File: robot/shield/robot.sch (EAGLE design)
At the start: 18 parts, among them IC1 LM386N-1, M2 ARDUINO_R3_ICSP, X1 22-23-2021, X2 22-23-2021, X3 22-23-2031, X4 22-23-2031, X5 22-23-2051

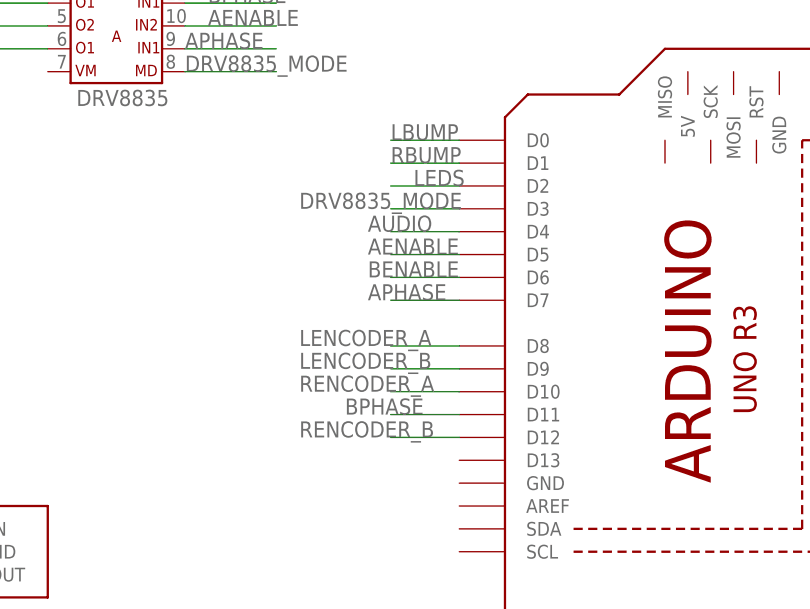
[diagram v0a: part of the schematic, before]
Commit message: Update pin assignments; layout
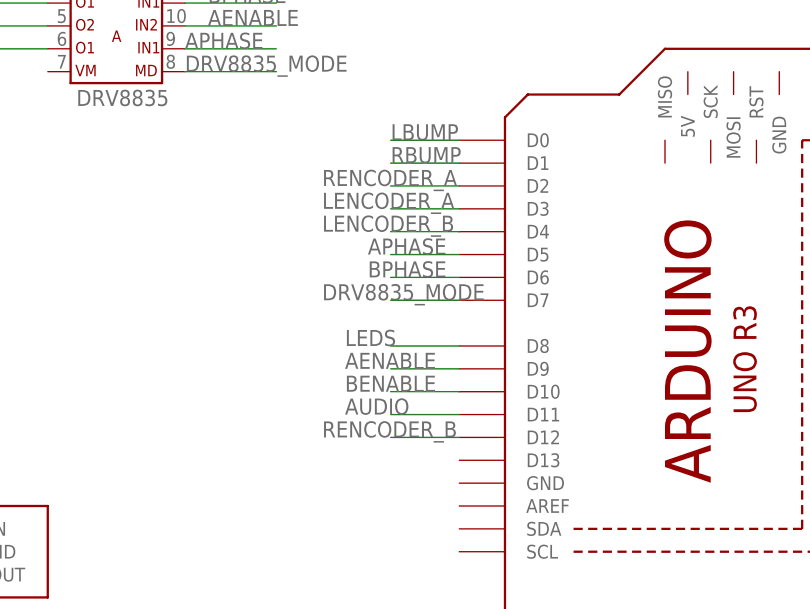
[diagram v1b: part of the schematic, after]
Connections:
- net AENABLE: now also M2.D9; no longer M2.D5
- net APHASE: now also M2.D5; no longer M2.D7
- net AUDIO: now also M2.D11; no longer M2.D4
- net BENABLE: now also M2.D10; no longer M2.D6
- net BPHASE: now also M2.D6; no longer M2.D11
- net DRV8835_MODE: now also M2.D7; no longer M2.D3
- net LEDS: now also M2.D8; no longer M2.D2
- net LENCODER_A: now also M2.D3; no longer M2.D8
- net LENCODER_B: now also M2.D4; no longer M2.D9
- net RENCODER_A: now also M2.D2; no longer M2.D10
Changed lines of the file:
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@@
 </segment>
 <segment>
-<wire x1="68.58" y1="73.66" x2="60.96" y2="73.66" width="0.1524" layer="91"/>
-<label x="50.8" y="73.66" size="1.778" layer="95"/>
-<pinref part="M2" gate="G$1" pin="D9"/>
+<wire x1="68.58" y1="88.9" x2="60.96" y2="88.9" width="0.1524" layer="91"/>
+<label x="53.34" y="88.9" size="1.778" layer="95"/>
+<pinref part="M2" gate="G$1" pin="D4"/>
 </segment>
 </net>
@@
 </segment>
 <segment>
-<wire x1="68.58" y1="76.2" x2="60.96" y2="76.2" width="0.1524" layer="91"/>
-<label x="50.8" y="76.2" size="1.778" layer="95"/>
-<pinref part="M2" gate="G$1" pin="D8"/>
+<wire x1="68.58" y1="91.44" x2="60.96" y2="91.44" width="0.1524" layer="91"/>
+<label x="53.34" y="91.44" size="1.778" layer="95"/>
+<pinref part="M2" gate="G$1" pin="D3"/>
 </segment>
 </net>
@@
 </segment>
 <segment>
-<wire x1="68.58" y1="71.12" x2="60.96" y2="71.12" width="0.1524" layer="91"/>
-<label x="50.8" y="71.12" size="1.778" layer="95"/>
-<pinref part="M2" gate="G$1" pin="D10"/>
+<wire x1="68.58" y1="93.98" x2="60.96" y2="93.98" width="0.1524" layer="91"/>
+<label x="53.34" y="93.98" size="1.778" layer="95"/>
+<pinref part="M2" gate="G$1" pin="D2"/>
 </segment>
 </net>
@@
 <segment>
 <wire x1="68.58" y1="66.04" x2="60.96" y2="66.04" width="0.1524" layer="91"/>
-<label x="50.8" y="66.04" size="1.778" layer="95"/>
+<label x="53.34" y="66.04" size="1.778" layer="95"/>
 <pinref part="M2" gate="G$1" pin="D12"/>
 </segment>
@@
 </segment>
 <segment>
-<wire x1="68.58" y1="88.9" x2="60.96" y2="88.9" width="0.1524" layer="91"/>
-<label x="58.42" y="88.9" size="1.778" layer="95"/>
-<pinref part="M2" gate="G$1" pin="D4"/>
+<wire x1="68.58" y1="68.58" x2="60.96" y2="68.58" width="0.1524" layer="91"/>
+<label x="55.88" y="68.58" size="1.778" layer="95"/>
+<pinref part="M2" gate="G$1" pin="D11"/>
 </segment>
 </net>
@@
 </segment>
 <segment>
-<wire x1="68.58" y1="93.98" x2="60.96" y2="93.98" width="0.1524" layer="91"/>
-<label x="63.5" y="93.98" size="1.778" layer="95"/>
-<pinref part="M2" gate="G$1" pin="D2"/>
+<wire x1="68.58" y1="76.2" x2="60.96" y2="76.2" width="0.1524" layer="91"/>
+<label x="55.88" y="76.2" size="1.778" layer="95"/>
+<pinref part="M2" gate="G$1" pin="D8"/>
 </segment>
 </net>
@@
 </segment>
 <segment>
-<wire x1="68.58" y1="91.44" x2="60.96" y2="91.44" width="0.1524" layer="91"/>
-<label x="50.8" y="91.44" size="1.778" layer="95"/>
-<pinref part="M2" gate="G$1" pin="D3"/>
+<wire x1="68.58" y1="81.28" x2="60.96" y2="81.28" width="0.1524" layer="91"/>
+<label x="53.34" y="81.28" size="1.778" layer="95"/>
+<pinref part="M2" gate="G$1" pin="D7"/>
 </segment>
 </net>
@@
 </segment>
 <segment>
-<wire x1="68.58" y1="81.28" x2="60.96" y2="81.28" width="0.1524" layer="91"/>
-<label x="58.42" y="81.28" size="1.778" layer="95"/>
-<pinref part="M2" gate="G$1" pin="D7"/>
+<wire x1="68.58" y1="86.36" x2="60.96" y2="86.36" width="0.1524" layer="91"/>
+<label x="58.42" y="86.36" size="1.778" layer="95"/>
+<pinref part="M2" gate="G$1" pin="D5"/>
 </segment>
 </net>
@@
 </segment>
 <segment>
-<wire x1="68.58" y1="86.36" x2="60.96" y2="86.36" width="0.1524" layer="91"/>
-<label x="58.42" y="86.36" size="1.778" layer="95"/>
-<pinref part="M2" gate="G$1" pin="D5"/>
+<wire x1="68.58" y1="73.66" x2="60.96" y2="73.66" width="0.1524" layer="91"/>
+<label x="55.88" y="73.66" size="1.778" layer="95"/>
+<pinref part="M2" gate="G$1" pin="D9"/>
 </segment>
 </net>
@@
 </segment>
 <segment>
-<wire x1="68.58" y1="68.58" x2="60.96" y2="68.58" width="0.1524" layer="91"/>
-<label x="55.88" y="68.58" size="1.778" layer="95"/>
-<pinref part="M2" gate="G$1" pin="D11"/>
+<wire x1="68.58" y1="83.82" x2="60.96" y2="83.82" width="0.1524" layer="91"/>
+<label x="58.42" y="83.82" size="1.778" layer="95"/>
+<pinref part="M2" gate="G$1" pin="D6"/>
 </segment>
 </net>
@@
 </segment>
 <segment>
-<wire x1="68.58" y1="83.82" x2="60.96" y2="83.82" width="0.1524" layer="91"/>
-<label x="58.42" y="83.82" size="1.778" layer="95"/>
-<pinref part="M2" gate="G$1" pin="D6"/>
-</segment>
-</net>
+<wire x1="68.58" y1="71.12" x2="60.96" y2="71.12" width="0.1524" layer="91"/>
+<label x="55.88" y="71.12" size="1.778" layer="95"/>
+<pinref part="M2" gate="G$1" pin="D10"/>
+</segment>
+</net>

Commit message: Updates to schematic and layout
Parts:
- removed R4, R5: 10K, adafruit:R-US_V234/12
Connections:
- net +5V: no longer R4.2, R5.2
- net BATLEVEL: now also M2.A3; no longer M2.A0
- net LBUMP: no longer R4.1
- net LINE1: now also M2.A0; no longer M2.A1
- net LINE2: now also M2.A1; no longer M2.A2
- net LINE3: now also M2.A2; no longer M2.A3
- net RBUMP: no longer R5.1
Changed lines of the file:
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@@
 <?xml version="1.0" encoding="utf-8"?>
 <!DOCTYPE eagle SYSTEM "eagle.dtd">
-<eagle version="6.6.0">
+<eagle version="7.0.0">
 <drawing>
 <settings>
@@
 <part name="X6" library="con-molex" deviceset="22-23-2061" device=""/>
 <part name="X7" library="con-molex" deviceset="22-23-2061" device=""/>
-<part name="R4" library="adafruit" deviceset="R-US_" device="V234/12" value="10K"/>
-<part name="R5" library="adafruit" deviceset="R-US_" device="V234/12" value="10K"/>
 <part name="GND13" library="supply1" deviceset="GND" device=""/>
-<part name="P+8" library="supply1" deviceset="+5V" device=""/>
 </parts>
 <sheets>
@@
 <instance part="X7" gate="-5" x="-17.78" y="129.54" rot="R180"/>
 <instance part="X7" gate="-6" x="-17.78" y="132.08" rot="R180"/>
-<instance part="R4" gate="G$1" x="73.66" y="154.94" rot="R90"/>
-<instance part="R5" gate="G$1" x="66.04" y="154.94" rot="R90"/>
 <instance part="GND13" gate="1" x="83.82" y="137.16"/>
-<instance part="P+8" gate="1" x="66.04" y="165.1"/>
 </instances>
 <busses>
@@
 <wire x1="40.64" y1="119.38" x2="40.64" y2="129.54" width="0.1524" layer="91"/>
 </segment>
-<segment>
-<pinref part="P+8" gate="1" pin="+5V"/>
-<wire x1="66.04" y1="162.56" x2="66.04" y2="160.02" width="0.1524" layer="91"/>
-<pinref part="R4" gate="G$1" pin="2"/>
-<wire x1="66.04" y1="160.02" x2="73.66" y2="160.02" width="0.1524" layer="91"/>
-<pinref part="R5" gate="G$1" pin="2"/>
-<junction x="66.04" y="160.02"/>
-</segment>
 </net>
 <net name="VBAT" class="2">
@@
 </segment>
 <segment>
+<wire x1="129.54" y1="88.9" x2="137.16" y2="88.9" width="0.1524" layer="91"/>
+<label x="129.54" y="88.9" size="1.778" layer="95"/>
+<pinref part="M2" gate="G$1" pin="A0"/>
+</segment>
+</net>
+<net name="LINE2" class="0">
+<segment>
+<wire x1="-17.78" y1="22.86" x2="-7.62" y2="22.86" width="0.1524" layer="91"/>
+<label x="-12.7" y="22.86" size="1.778" layer="95"/>
+<pinref part="X5" gate="-4" pin="S"/>
+</segment>
+<segment>
 <wire x1="129.54" y1="91.44" x2="137.16" y2="91.44" width="0.1524" layer="91"/>
 <label x="129.54" y="91.44" size="1.778" layer="95"/>
@@
 </segment>
 </net>
-<net name="LINE2" class="0">
-<segment>
-<wire x1="-17.78" y1="22.86" x2="-7.62" y2="22.86" width="0.1524" layer="91"/>
-<label x="-12.7" y="22.86" size="1.778" layer="95"/>
-<pinref part="X5" gate="-4" pin="S"/>
+<net name="LINE3" class="0">
+<segment>
+<wire x1="-17.78" y1="25.4" x2="-7.62" y2="25.4" width="0.1524" layer="91"/>
+<label x="-12.7" y="25.4" size="1.778" layer="95"/>
+<pinref part="X5" gate="-5" pin="S"/>
 </segment>
 <segment>
@@
 <label x="129.54" y="93.98" size="1.778" layer="95"/>
 <pinref part="M2" gate="G$1" pin="A2"/>
-</segment>
-</net>
-<net name="LINE3" class="0">
-<segment>
-<wire x1="-17.78" y1="25.4" x2="-7.62" y2="25.4" width="0.1524" layer="91"/>
-<label x="-12.7" y="25.4" size="1.778" layer="95"/>
-<pinref part="X5" gate="-5" pin="S"/>
-</segment>
-<segment>
-<wire x1="129.54" y1="96.52" x2="137.16" y2="96.52" width="0.1524" layer="91"/>
-<label x="129.54" y="96.52" size="1.778" layer="95"/>
-<pinref part="M2" gate="G$1" pin="A3"/>
 </segment>
 </net>
@@
 </segment>
 <segment>
-<wire x1="129.54" y1="88.9" x2="137.16" y2="88.9" width="0.1524" layer="91"/>
-<label x="129.54" y="88.9" size="1.778" layer="95"/>
-<pinref part="M2" gate="G$1" pin="A0"/>
+<wire x1="129.54" y1="96.52" x2="137.16" y2="96.52" width="0.1524" layer="91"/>
+<label x="129.54" y="96.52" size="1.778" layer="95"/>
+<pinref part="M2" gate="G$1" pin="A3"/>
 </segment>
 </net>
@@
 <net name="LBUMP" class="0">
 <segment>
-<pinref part="R4" gate="G$1" pin="1"/>
 <pinref part="X4" gate="-1" pin="S"/>
-<wire x1="73.66" y1="149.86" x2="86.36" y2="149.86" width="0.1524" layer="91"/>
-<label x="78.74" y="149.86" size="1.778" layer="95"/>
+<wire x1="76.2" y1="149.86" x2="86.36" y2="149.86" width="0.1524" layer="91"/>
+<label x="73.66" y="149.86" size="1.778" layer="95"/>
 </segment>
 <segment>
@@
 <net name="RBUMP" class="0">
 <segment>
-<pinref part="R5" gate="G$1" pin="1"/>
-<wire x1="66.04" y1="149.86" x2="66.04" y2="144.78" width="0.1524" layer="91"/>
-<wire x1="66.04" y1="144.78" x2="86.36" y2="144.78" width="0.1524" layer="91"/>
+<wire x1="76.2" y1="144.78" x2="86.36" y2="144.78" width="0.1524" layer="91"/>
 <pinref part="X4" gate="-3" pin="S"/>
 <label x="73.66" y="144.78" size="1.778" layer="95"/>
